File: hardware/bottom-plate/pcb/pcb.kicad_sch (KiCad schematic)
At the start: 66 parts, among them SW1 MT-0-102-A101-M200-RS+PJ, SW2 TS4535TP 250GF 009, SW3 TS4535TP 250GF 009

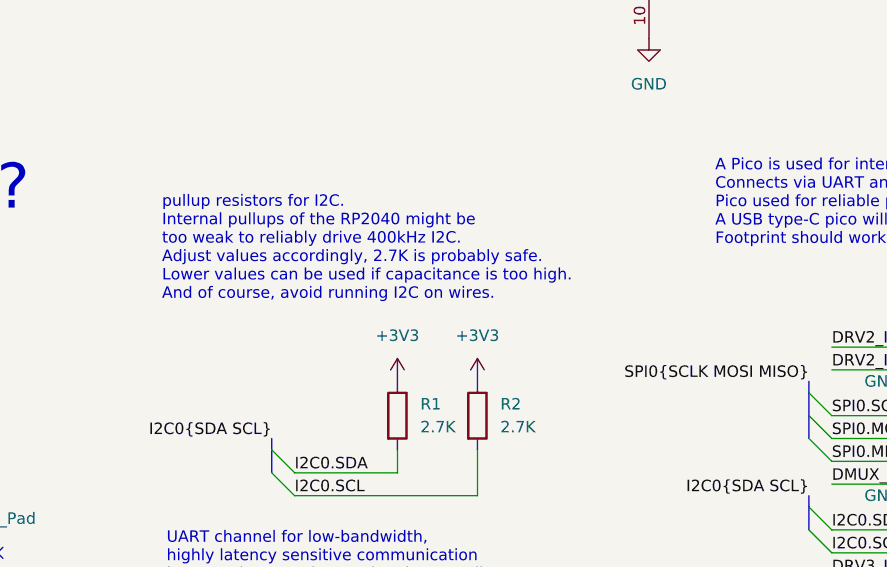
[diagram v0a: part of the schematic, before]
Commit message: Revert "fixed naming and structure"
This reverts commit 85cb8a6d80e828be1fe4c6e36d316d3d322d80a6.
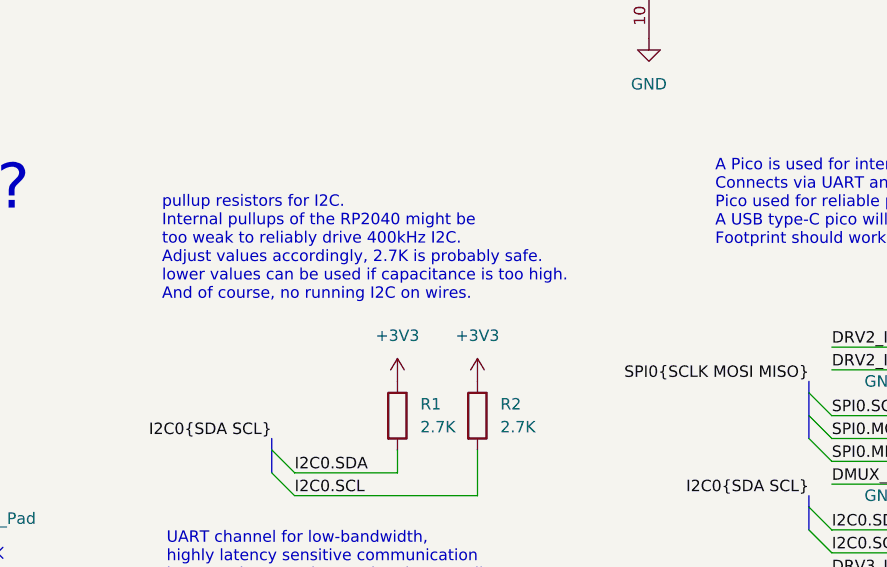
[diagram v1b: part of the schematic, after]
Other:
- note added: "pullup resistors for I2C. Internal pullups of the RP2040 might be too weak to reliably drive 400kHz I2C. Adjust values accordingly, 2.7K is probably safe. lower values can be used if capacitance is too high. And of course, no running I2C on wires."
- note removed: "pullup resistors for I2C. Internal pullups of the RP2040 might be too weak to reliably drive 400kHz I2C. Adjust values accordingly, 2.7K is probably safe. Lower values can be used if capacitance is too high. And of course, avoid running I2C on wires."
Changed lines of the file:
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@@
 		)
 	)
-	(text "pullup resistors for I2C.\nInternal pullups of the RP2040 might be\ntoo weak to reliably drive 400kHz I2C.\nAdjust values accordingly, 2.7K is probably safe.\nLower values can be used if capacitance is too high.\nAnd of course, avoid running I2C on wires."
+	(text "pullup resistors for I2C.\nInternal pullups of the RP2040 might be\ntoo weak to reliably drive 400kHz I2C.\nAdjust values accordingly, 2.7K is probably safe.\nlower values can be used if capacitance is too high.\nAnd of course, no running I2C on wires."
 		(exclude_from_sim no)
 		(at 100.838 202.438 0)

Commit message: fixed naming and structure
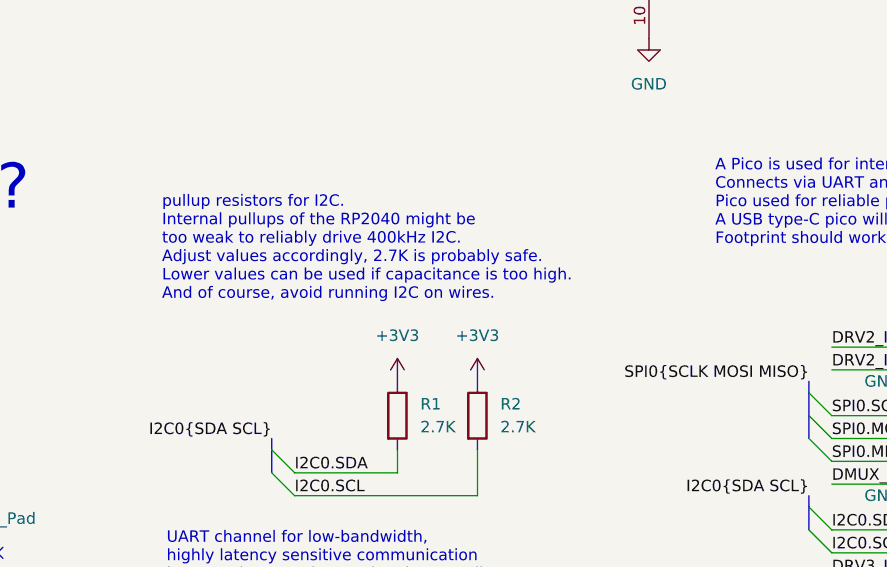
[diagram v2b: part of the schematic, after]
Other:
- note added: "pullup resistors for I2C. Internal pullups of the RP2040 might be too weak to reliably drive 400kHz I2C. Adjust values accordingly, 2.7K is probably safe. Lower values can be used if capacitance is too high. And of course, avoid running I2C on wires."
- note removed: "pullup resistors for I2C. Internal pullups of the RP2040 might be too weak to reliably drive 400kHz I2C. Adjust values accordingly, 2.7K is probably safe. lower values can be used if capacitance is too high. And of course, no running I2C on wires."
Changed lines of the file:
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@@
 		)
 	)
-	(text "pullup resistors for I2C.\nInternal pullups of the RP2040 might be\ntoo weak to reliably drive 400kHz I2C.\nAdjust values accordingly, 2.7K is probably safe.\nlower values can be used if capacitance is too high.\nAnd of course, no running I2C on wires."
+	(text "pullup resistors for I2C.\nInternal pullups of the RP2040 might be\ntoo weak to reliably drive 400kHz I2C.\nAdjust values accordingly, 2.7K is probably safe.\nLower values can be used if capacitance is too high.\nAnd of course, avoid running I2C on wires."
 		(exclude_from_sim no)
 		(at 100.838 202.438 0)
